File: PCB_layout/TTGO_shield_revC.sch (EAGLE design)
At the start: 27 parts

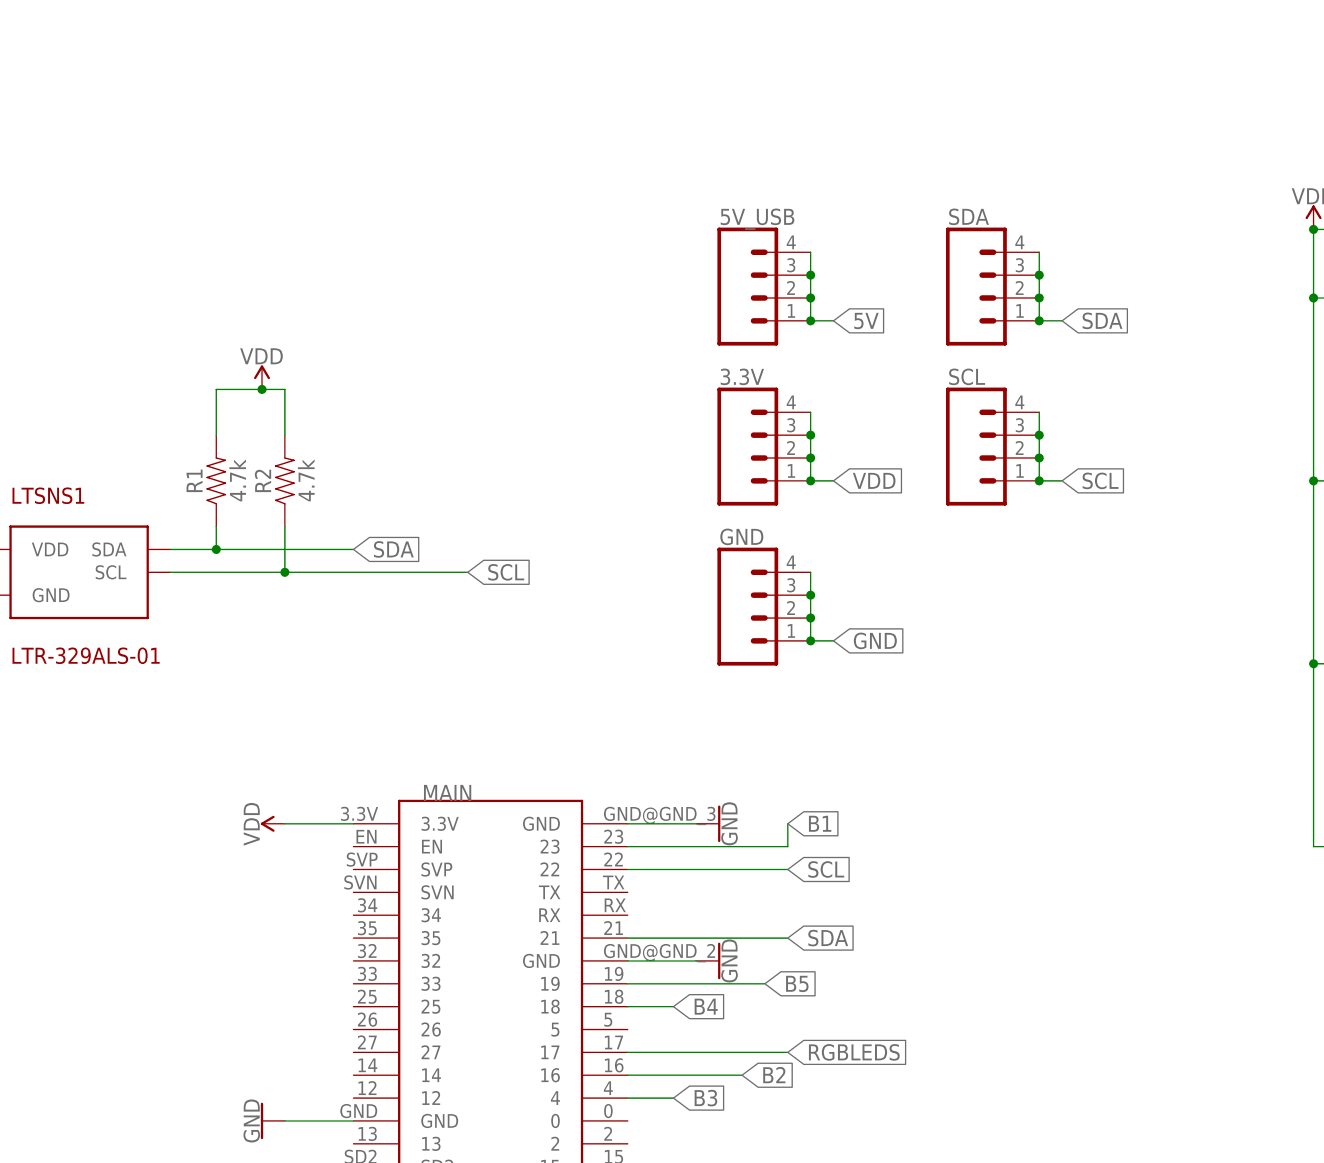
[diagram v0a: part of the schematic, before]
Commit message: corrected capsense pads
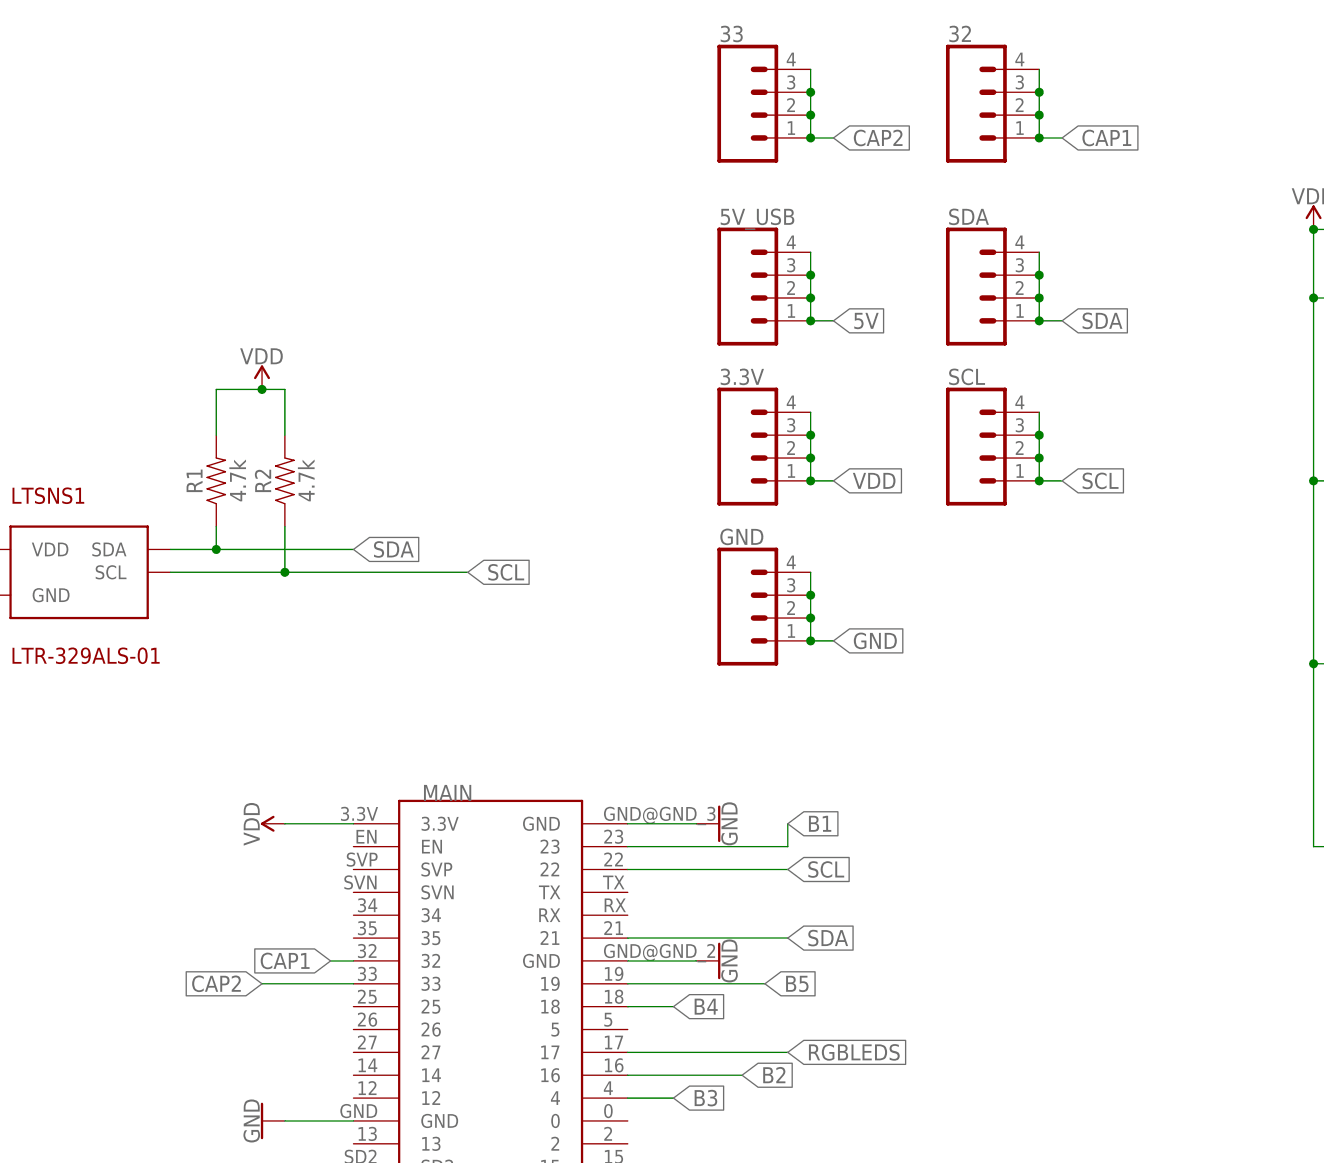
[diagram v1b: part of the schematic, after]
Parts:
- added 32, 33: (no value), SparkFun-Connectors:CONN_041X04_NO_SILK
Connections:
- new net CAP1: 32.1, 32.2, 32.3, 32.4, MAIN.32
- new net CAP2: 33.1, 33.2, 33.3, 33.4, MAIN.33
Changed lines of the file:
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@@
 <part name="SUPPLY7" library="SparkFun-PowerSymbols" library_urn="urn:adsk.eagle:library:530" deviceset="VDD" device=""/>
 <part name="SUPPLY6" library="SparkFun-PowerSymbols" library_urn="urn:adsk.eagle:library:530" deviceset="VDD" device=""/>
+<part name="32" library="SparkFun-Connectors" library_urn="urn:adsk.eagle:library:513" deviceset="CONN_04" device="1X04_NO_SILK" package3d_urn="urn:adsk.eagle:package:38094/1"/>
+<part name="33" library="SparkFun-Connectors" library_urn="urn:adsk.eagle:library:513" deviceset="CONN_04" device="1X04_NO_SILK" package3d_urn="urn:adsk.eagle:package:38094/1"/>
 </parts>
 <sheets>
@@
 <instance part="SUPPLY7" gate="VDD" x="88.9" y="0"/>
 <instance part="SUPPLY6" gate="VDD" x="-58.42" y="55.88"/>
+<instance part="32" gate="G$1" x="73.66" y="134.62"/>
+<instance part="33" gate="G$1" x="48.26" y="134.62"/>
 </instances>
 <busses>
@@
 </segment>
 </net>
+<net name="CAP1" class="0">
+<segment>
+<pinref part="32" gate="G$1" pin="4"/>
+<pinref part="32" gate="G$1" pin="3"/>
+<wire x1="78.74" y1="139.7" x2="78.74" y2="137.16" width="0.1524" layer="91"/>
+<pinref part="32" gate="G$1" pin="2"/>
+<wire x1="78.74" y1="134.62" x2="78.74" y2="137.16" width="0.1524" layer="91"/>
+<junction x="78.74" y="137.16"/>
+<pinref part="32" gate="G$1" pin="1"/>
+<wire x1="78.74" y1="134.62" x2="78.74" y2="132.08" width="0.1524" layer="91"/>
+<junction x="78.74" y="134.62"/>
+<wire x1="78.74" y1="132.08" x2="81.28" y2="132.08" width="0.1524" layer="91"/>
+<junction x="78.74" y="132.08"/>
+<label x="81.28" y="132.08" size="1.778" layer="95" xref="yes"/>
+</segment>
+<segment>
+<pinref part="MAIN" gate="G$1" pin="32"/>
+<wire x1="2.54" y1="40.64" x2="0" y2="40.64" width="0.1524" layer="91"/>
+<label x="0" y="40.64" size="1.778" layer="95" rot="R180" xref="yes"/>
+</segment>
+</net>
+<net name="CAP2" class="0">
+<segment>
+<pinref part="33" gate="G$1" pin="4"/>
+<pinref part="33" gate="G$1" pin="3"/>
+<wire x1="53.34" y1="139.7" x2="53.34" y2="137.16" width="0.1524" layer="91"/>
+<pinref part="33" gate="G$1" pin="2"/>
+<wire x1="53.34" y1="137.16" x2="53.34" y2="134.62" width="0.1524" layer="91"/>
+<junction x="53.34" y="137.16"/>
+<pinref part="33" gate="G$1" pin="1"/>
+<wire x1="53.34" y1="134.62" x2="53.34" y2="132.08" width="0.1524" layer="91"/>
+<junction x="53.34" y="134.62"/>
+<wire x1="53.34" y1="132.08" x2="55.88" y2="132.08" width="0.1524" layer="91"/>
+<junction x="53.34" y="132.08"/>
+<label x="55.88" y="132.08" size="1.778" layer="95" xref="yes"/>
+</segment>
+<segment>
+<pinref part="MAIN" gate="G$1" pin="33"/>
+<wire x1="2.54" y1="38.1" x2="-7.62" y2="38.1" width="0.1524" layer="91"/>
+<label x="-7.62" y="38.1" size="1.778" layer="95" rot="R180" xref="yes"/>
+</segment>
+</net>
